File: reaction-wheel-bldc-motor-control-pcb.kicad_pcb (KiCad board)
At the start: 2 copper layers, 48.6 x 49.5 mm, 48 parts, among them J1 Conn_01x04_Pin, J2 Conn_01x04_Pin, J3 Conn_01x03_Pin, J4 USB_C_Receptacle_USB2.0_16P, J5 Conn_01x04_Pin, J6 Conn_01x06_Pin, SW1 SW_SPST, U1 USBLC6-2SC6, U2 STM32G431CBUx, U4 DRV8311H, U5 SN65HVD231, U6 TPS562200, Y1 16MHz

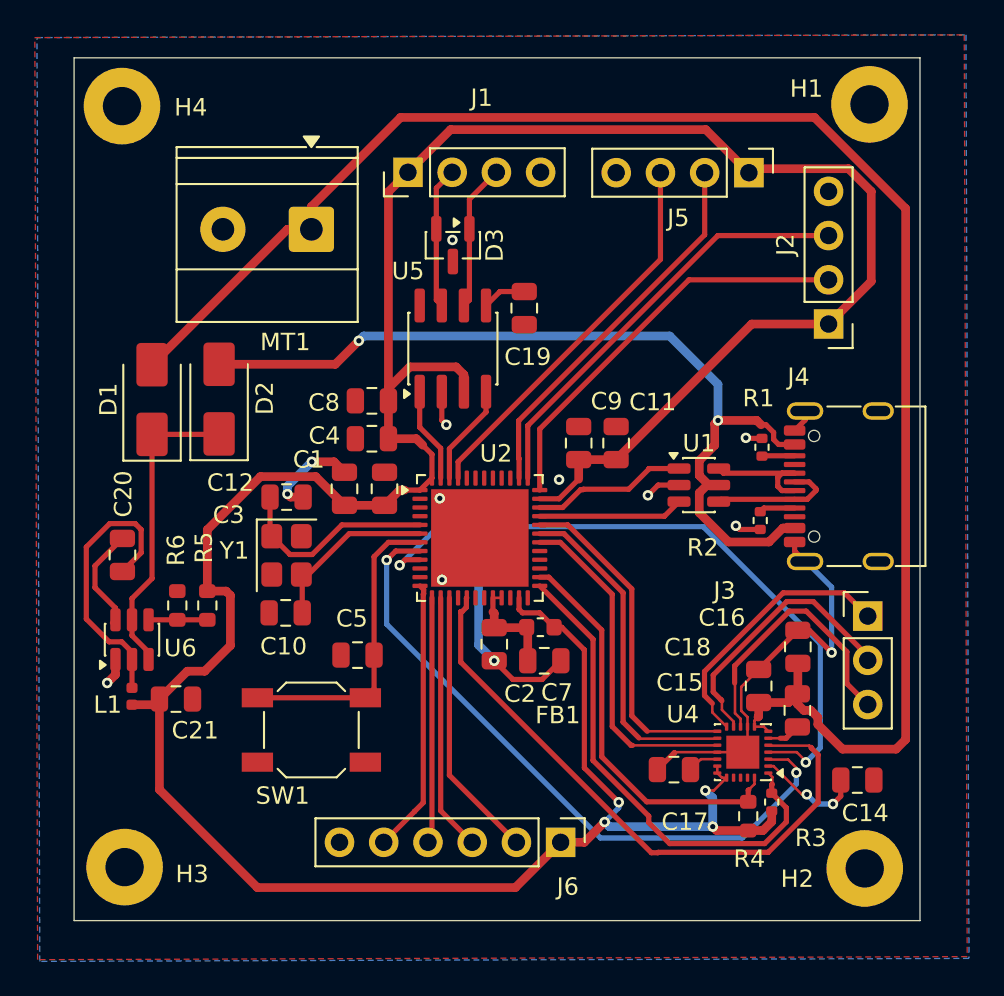
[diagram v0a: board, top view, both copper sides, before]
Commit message: changed stm32 from u6 to t6
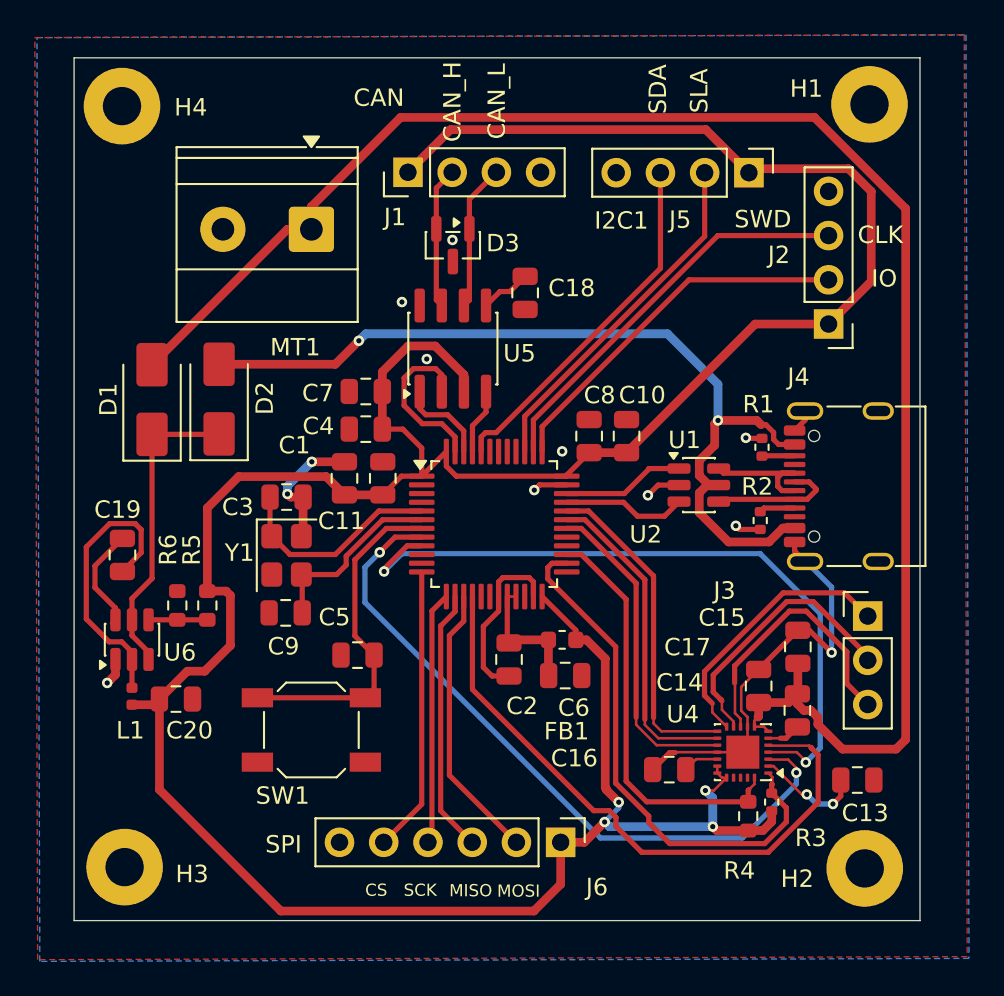
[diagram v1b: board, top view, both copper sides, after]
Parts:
- added G***: LOGO, LOGO, B.Cu at (142.4, 92.6)
- U2: value STM32G431CBUx -> STM32G431CBTx; footprint Package_DFN_QFN:QFN-48-1EP_7x7mm_P0.5mm_EP5.6x5.6mm -> Package_QFP:LQFP-48_7x7mm_P0.5mm
- moved C6 1.47 mm to (145.6, 99.9)
- moved FB1 1.45 mm to (145.4, 97.8)
- moved C2 1.22 mm to (142.3, 99.0)
- moved U2 1.15 mm to (141.5, 91.2)
- moved C18 0.88 mm to (143.3, 77.9)
- moved C10 0.72 mm to (149.1, 86.2)
- moved C8 0.72 mm to (146.9, 86.2)
- moved C4 0.65 mm to (134.1, 85.8)
- moved C7 0.64 mm to (134.1, 83.6)
- moved C11 0.61 mm to (135.1, 88.6)
- moved C1 0.60 mm to (132.9, 88.6)
- moved C16 0.27 mm to (151.6, 105.3)
- renumbered C11 to C10, C12 to C11, C14 to C13, C15 to C14, C16 to C15, C17 to C16, C18 to C17, C19 to C18, C20 to C19, C21 to C20, C7 to C6, C8 to C7, C9 to C8, C10 to C9
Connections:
- U2 pad 16: unconnected-(U2-PC4-Pad16) -> /PB0
- U2 pad 17: /PB0 -> unconnected-(U2-PB1-Pad17)
- U2 pad 19: unconnected-(U2-PB2-Pad19) -> GND
- U2 pad 23: +3.3V -> GND
- U2 pad 24: unconnected-(U2-PB11-Pad24) -> +3.3V
- U2 pad 25: /FAULT -> unconnected-(U2-PB11-Pad25)
- U2 pad 26: /SLEEP -> /FAULT
- U2 pad 27: unconnected-(U2-PB14-Pad27) -> /SLEEP
- U2 pad 35: +3.3V -> GND
- U2 pad 36: /SWDIO -> +3.3V
- U2 pad 37: /SWDCLK -> /SWDIO
- U2 pad 38: /I2C1_SCL -> /SWDCLK
- U2 pad 39: unconnected-(U2-PC10-Pad39) -> /I2C1_SCL
- U2 pad 44: unconnected-(U2-PB6-Pad44) -> /I2C1_SDA
- U2 pad 45: /I2C1_SDA -> /CAN_RX
- U2 pad 46: /CAN_RX -> /CAN_TX
- U2 pad 47: /CAN_TX -> GND
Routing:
- net GND: track 51.4 -> 60.6 mm, vias 13 -> 12
- net +3.3V: track 183.2 -> 180.1 mm
- net /PA1: track 38.8 -> 41.1 mm
- net /SWDIO: track 23.6 -> 21.4 mm
- net /CAN_RX: track 5.83 -> 3.76 mm
- net /FAULT: track 28.4 -> 30.4 mm
- net /PA0: track 38.4 -> 40.4 mm
- net /NRST: track 17.5 -> 19.4 mm
- net /USB_D+: track 8.95 -> 7.07 mm
- net /I2C1_SDA: track 22.4 -> 20.6 mm
- net /I2C1_SCL: track 22.0 -> 20.3 mm
- net /SWDCLK: track 24.8 -> 23.1 mm
- net +3.3VA: track 6.07 -> 7.59 mm
- net /USB_D-: track 8.35 -> 7.13 mm
- net /PA8: track 19.5 -> 18.6 mm
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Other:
- board text added: "CAN"
- board text added: "CAN_H"
- board text added: "CAN_L"
- board text added: "CLK"
- board text added: "CS"
- board text added: "I2C1"
- board text added: "IO"
- board text added: "MISO"
- board text added: "MOSI"
- board text added: "SCK"
- board text added: "SDA"
- board text added: "SLA"
- board text added: "SPI"
- board text added: "SWD"

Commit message: complete drv8311 connections
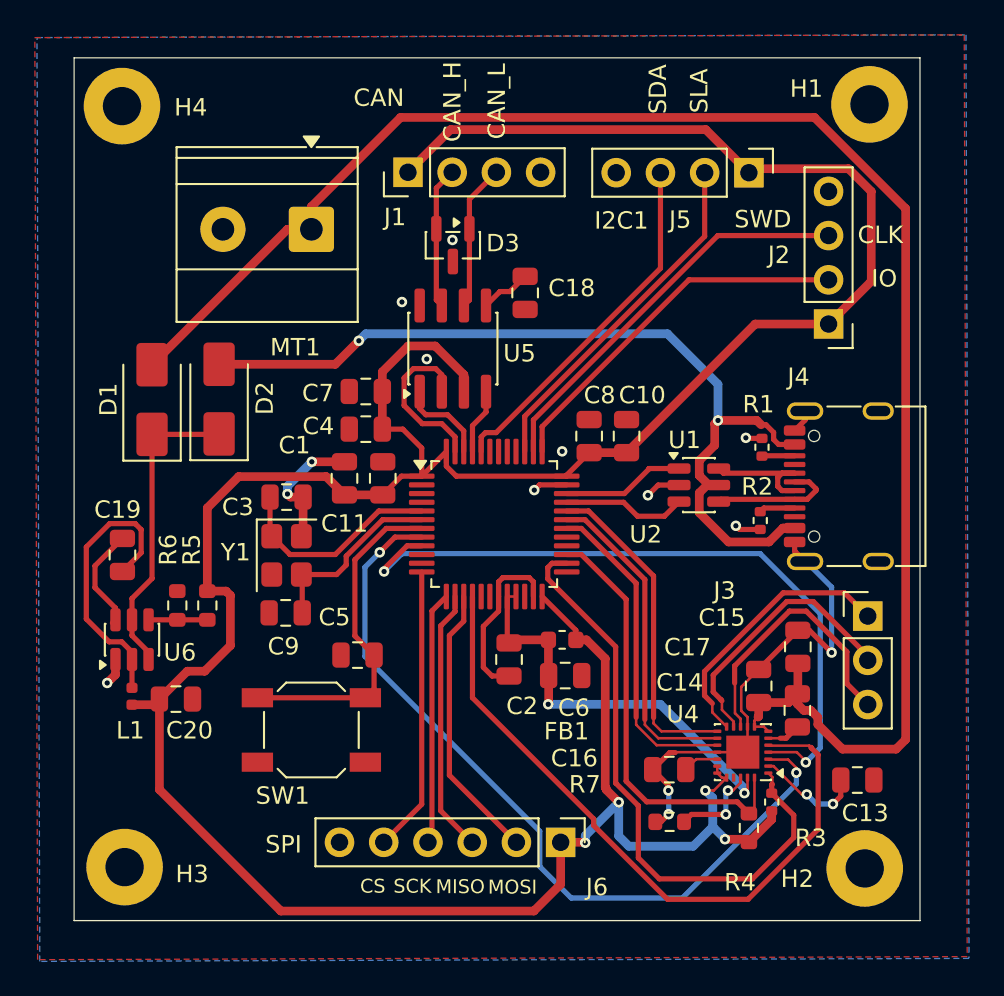
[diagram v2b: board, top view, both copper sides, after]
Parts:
- added R7: 47k, Resistor_SMD:R_0603_1608Metric, F.Cu at (151.6, 108.3)
- moved R4 0.68 mm to (156.1, 108.7)
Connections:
- U4 pad 22: unconnected-(U4-SLEW-Pad22) -> Net-(U4-SLEW)
- U4 pad 23: unconnected-(U4-MODE-Pad23) -> +3.3VA
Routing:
- net +3.3VA: track 7.59 -> 23.8 mm, vias 0 -> 2
- net /PA0: track 40.4 -> 46.3 mm
- net Net-(U4-SLEW): track 0.00 -> 5.20 mm, vias 0 -> 2
- net /FAULT: track 30.4 -> 34.8 mm
- net GND: track 60.6 -> 64.4 mm, vias 12 -> 14
- net /PB0: track 36.4 -> 39.7 mm
- net +3.3V: track 180.1 -> 182.4 mm
- net /SLEEP: track 24.0 -> 24.9 mm
